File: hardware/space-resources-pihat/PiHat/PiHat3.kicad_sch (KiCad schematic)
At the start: 44 parts, among them J1 GPIO, J10 Conn_01x02_Socket, J11 Conn_01x03_Socket, J12 Conn_01x03_Socket, J13 Conn_01x03_Socket, J14 Conn_01x02_Socket, J2 Conn_01x02_Socket, J3 Conn_01x04_Socket, J4 Conn_01x04_Socket, J5 Conn_01x02_Socket, J6 Conn_01x02_Socket, J7 Conn_01x02_Socket, J8 Conn_01x04_Socket, J9 Conn_01x02_Socket, M1 AO3400A, M3 AO3400A, U1 TPS54560BDDA

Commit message: fix: Changed buck input and output caps for digikey stocked components
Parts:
- removed D3: SMAZ5V1-13-F, Diode_SMD:D_SMA, symbol Device:D_Zener
- C1, C2, C3: value 2.2u -> 10u; footprint Capacitor_SMD:C_0603_1608Metric -> Capacitor_SMD:C_1206_3216Metric_Pad1.33x1.80mm_HandSolder
- C11, C6, C8: footprint Capacitor_SMD:C_1808_4520Metric -> Capacitor_SMD:C_1210_3225Metric_Pad1.33x2.70mm_HandSolder
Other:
- note added: "https://webench.ti.com/appinfo/webench/scripts/SDP.cgi?ID=436553DDC7067EBB"
- note removed: "(https://webench.ti.com/appinfo/webench/scripts/SDP.cgi?ID=436553DDC7067EBB)"

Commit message: fix: Rectified layout to fit properly with Pi4, added various testpoints and optional i2c pullup resistors
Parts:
- removed J3: Conn_01x04_Socket, Connector_JST:JST_EH_B4B-EH-A_1x04_P2.50mm_Vertical, symbol Connector:Conn_01x04_Socket
- added J3: Conn_01x06_Socket, Connector_JST:JST_EH_B6B-EH-A_1x06_P2.50mm_Vertical, symbol Connector:Conn_01x06_Socket
- added TP1: TestPoint, symbol Connector:TestPoint
- renumbered L2 to L1
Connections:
- net 24V: now also TP1.1
- net 3V3: now also J3.3 (Pin_3)
- net 5V: now also J13.2 (Pin_2), J7.2 (Pin_2), J9.2 (Pin_2); no longer J13.1 (Pin_1), J7.1 (Pin_1), J9.1 (Pin_1)
- net GND: now also J10.1 (Pin_1), J13.1 (Pin_1), J14.1 (Pin_1), J3.4 (Pin_4); no longer J10.2 (Pin_2), J13.2 (Pin_2), J14.2 (Pin_2)
- net GPIO17: now also J3.5 (Pin_5)
- net GPIO19/PCM.FS: now also R11.2; no longer R2.2
- net GPIO20/PCM.DIN: no longer R11.2
- net GPIO26: now also R2.2
- net GPIO27: now also J3.6 (Pin_6)
- net GPIO2/SDA1: now also J3.2 (Pin_2)
- net GPIO3/SCL1: now also J3.1 (Pin_1)
- net at R13.1: now also J10.2 (Pin_2); no longer J10.1 (Pin_1)
- net at D2.2 (A), M1.3 (D): now also J7.1 (Pin_1); no longer J7.2 (Pin_2)
- net at M3.3 (D): now also J9.1 (Pin_1); no longer J9.2 (Pin_2)
- net at R15.1: now also J14.2 (Pin_2); no longer J14.1 (Pin_1)
- net BST: now reaches C4.1, U1.1 (BOOT)
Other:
- note added: "Test Points"
- moved on the sheet: J14, J4, L1

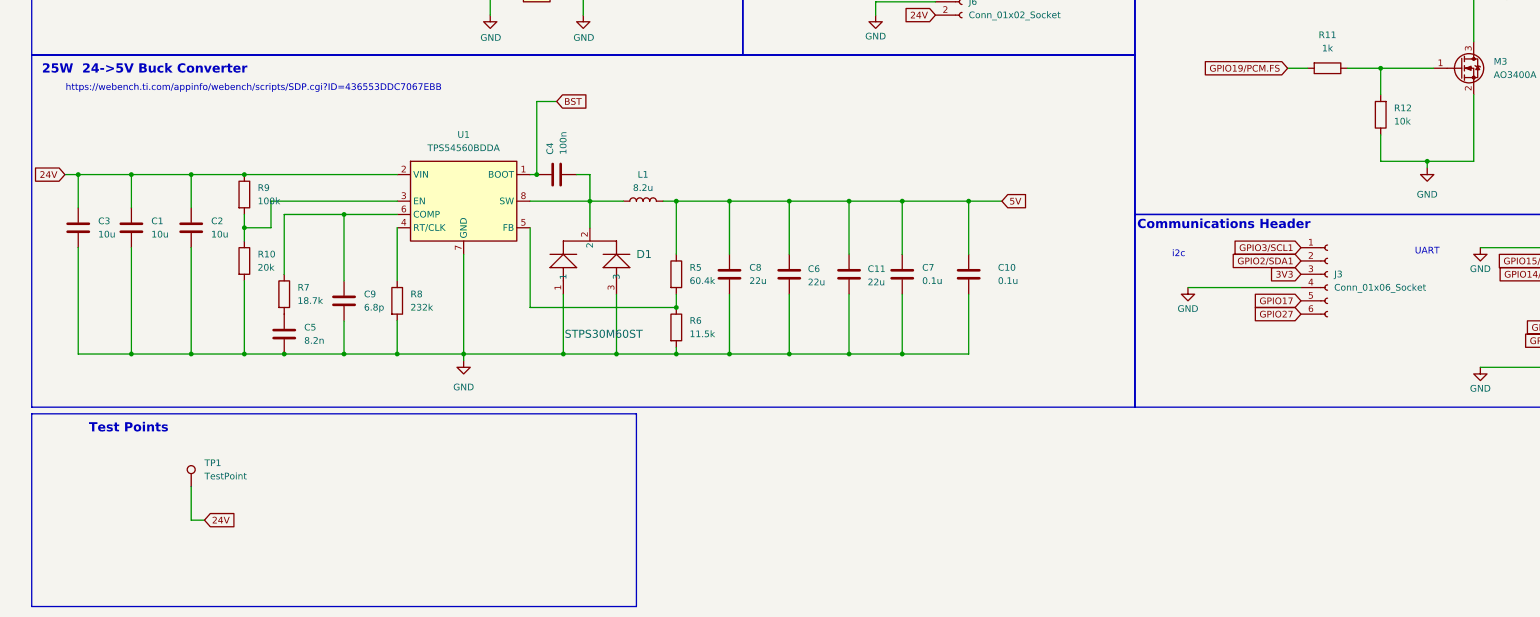
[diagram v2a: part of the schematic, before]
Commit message: small schematic changes
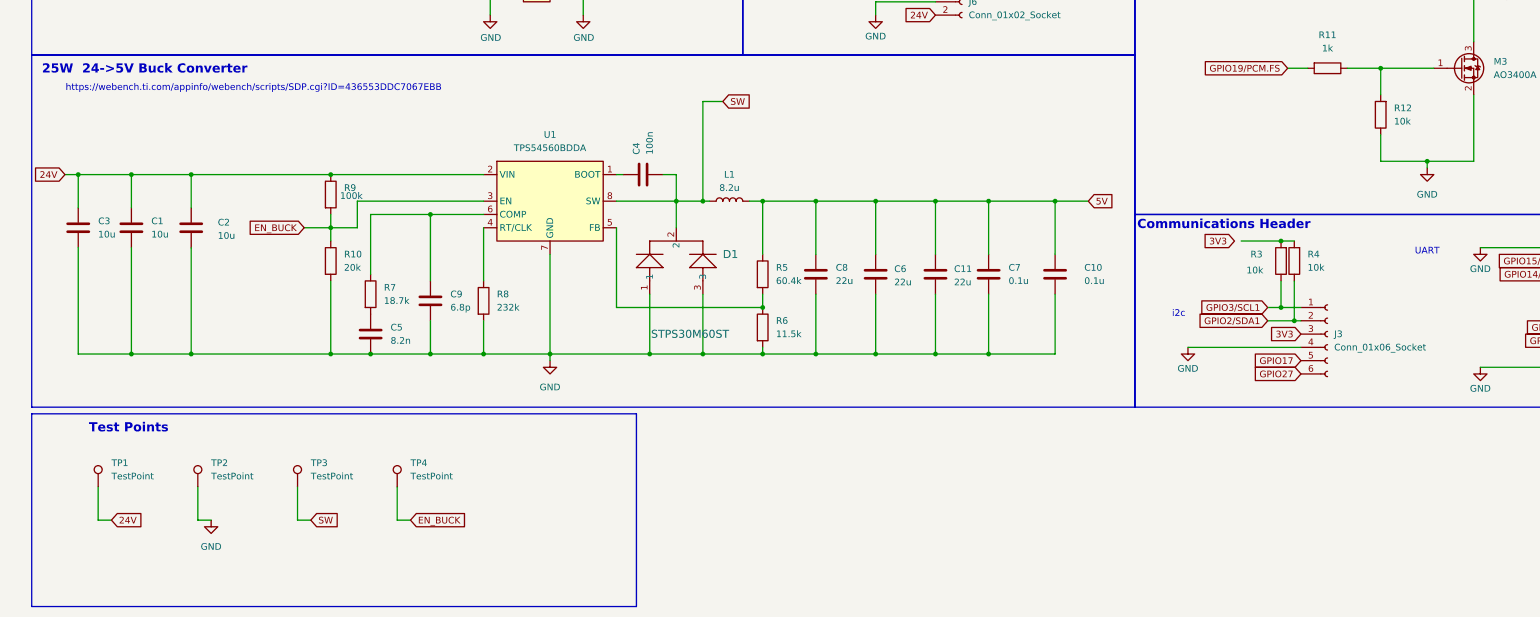
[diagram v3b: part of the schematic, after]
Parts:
- added R3, R4: 10k, Resistor_SMD:R_0603_1608Metric_Pad0.98x0.95mm_HandSolder, symbol Device:R
- added TP2: TestPoint, Connector_Pin:Pin_D1.0mm_L10.0mm, symbol Connector:TestPoint
- added TP3, TP4: TestPoint, Connector_PinHeader_1.00mm:PinHeader_1x01_P1.00mm_Vertical, symbol Connector:TestPoint
- TP1: footprint (none) -> Connector_Pin:Pin_D1.0mm_L10.0mm
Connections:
- net GND: now also TP2.1
- net GPIO2/SDA1: now also R4.1
- net GPIO3/SCL1: now also R3.1
- net SW: now reaches C4.2, D1.2, L1.1, U1.8 (SW)
- net SW: now also TP3.1
- net EN_BUCK: now reaches R10.1, R9.2, U1.3 (EN)
- net EN_BUCK: now also TP4.1
- net BST: no longer names the net of C4.1, U1.1 (BOOT)
- new net: R3.2, R4.2
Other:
- moved on the sheet: C10, C11, C4, C5, C6, C7, C8, C9, D1, J3, L1, R10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

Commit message: fix: Final touchups, ready for order
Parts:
- TP1, TP2: footprint Connector_Pin:Pin_D1.0mm_L10.0mm -> Connector_PinHeader_1.00mm:PinHeader_1x01_P1.00mm_Vertical
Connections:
- net 3V3: now also R3.2, R4.2
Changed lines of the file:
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@@
 	(global_label "3V3"
 		(shape input)
-		(at 243.84 123.19 180)
+		(at 245.11 123.19 180)
 		(fields_autoplaced yes)
 		(effects
@@
 		)
 		(property "Intersheetrefs" "${INTERSHEET_REFS}"
-			(at 237.2521 123.19 0)
+			(at 238.5221 123.19 0)
 			(effects
 				(font
@@
 	)
 	(symbol
+		(lib_id "Connector:TestPoint")
+		(at 26.67 170.18 0)
+		(unit 1)
+		(exclude_from_sim no)
+		(in_bom yes)
+		(on_board yes)
+		(dnp no)
+		(fields_autoplaced yes)
+		(property "Reference" "TP1"
+			(at 29.21 165.6079 0)
+			(effects
+				(font
+					(size 1.27 1.27)
+				)
+				(justify left)
+			)
+		)
+		(property "Value" "TestPoint"
+			(at 29.21 168.1479 0)
+			(effects
+				(font
+					(size 1.27 1.27)
+				)
+				(justify left)
+			)
+		)
+		(property "Footprint" "Connector_PinHeader_1.00mm:PinHeader_1x01_P1.00mm_Vertical"
+			(at 31.75 170.18 0)
+			(effects
+				(font
+					(size 1.27 1.27)
+				)
+				(hide yes)
+			)
+		)
+		(property "Datasheet" "~"
+			(at 31.75 170.18 0)
+			(effects
+				(font
+					(size 1.27 1.27)
+				)
+				(hide yes)
+			)
+		)
+		(property "Description" "test point"
+			(at 26.67 170.18 0)
+			(effects
+				(font
+					(size 1.27 1.27)
+				)
+				(hide yes)
+			)
+		)
+		(pin "1"
+		)
+		(instances
+			(project "PiHat3"
+				(path "/e63e39d7-6ac0-4ffd-8aa3-1841a4541b55"
+					(reference "TP1")
+					(unit 1)
+				)
+			)
+		)
+	)
+	(symbol
 		(lib_id "Device:R")
 		(at 78.74 133.35 0)
@@
 	)
 	(symbol
-		(lib_id "Connector:TestPoint")
-		(at 45.72 170.18 0)
-		(unit 1)
-		(exclude_from_sim no)
-		(in_bom yes)
-		(on_board yes)
-		(dnp no)
-		(fields_autoplaced yes)
-		(property "Reference" "TP2"
-			(at 48.26 165.6079 0)
-			(effects
-				(font
-					(size 1.27 1.27)
-				)
-				(justify left)
-			)
-		)
-		(property "Value" "TestPoint"
-			(at 48.26 168.1479 0)
-			(effects
-				(font
-					(size 1.27 1.27)
-				)
-				(justify left)
-			)
-		)
-		(property "Footprint" "Connector_Pin:Pin_D1.0mm_L10.0mm"
-			(at 50.8 170.18 0)
-			(effects
-				(font
-					(size 1.27 1.27)
-				)
-				(hide yes)
-			)
-		)
-		(property "Datasheet" "~"
-			(at 50.8 170.18 0)
-			(effects
-				(font
-					(size 1.27 1.27)
-				)
-				(hide yes)
-			)
-		)
-		(property "Description" "test point"
-			(at 45.72 170.18 0)
-			(effects
-				(font
-					(size 1.27 1.27)
-				)
-				(hide yes)
-			)
-		)
-		(pin "1"
-		)
-		(instances
-			(project "PiHat3"
-				(path "/e63e39d7-6ac0-4ffd-8aa3-1841a4541b55"
-					(reference "TP2")
-					(unit 1)
-				)
-			)
-		)
-	)
-	(symbol
 		(lib_id "Transistor_FET:AO3400A")
 		(at 287.02 90.17 0)
@@
 	)
 	(symbol
-		(lib_id "Connector:TestPoint")
-		(at 26.67 170.18 0)
+		(lib_id "Device:C")
+		(at 130.81 110.49 90)
 		(unit 1)
 		(exclude_from_sim no)
@@
 		(on_board yes)
 		(dnp no)
-		(fields_autoplaced yes)
-		(property "Reference" "TP1"
-			(at 29.21 165.6079 0)
+		(property "Reference" "C4"
+			(at 129.5399 106.68 0)
 			(effects
 				(font
@@
 			)
 		)
-		(property "Value" "TestPoint"
-			(at 29.21 168.1479 0)
+		(property "Value" "100n"
+			(at 132.0799 106.68 0)
 			(effects
 				(font
@@
 			)
 		)
-		(property "Footprint" "Connector_Pin:Pin_D1.0mm_L10.0mm"
-			(at 31.75 170.18 0)
+		(property "Footprint" "Capacitor_SMD:C_0603_1608Metric"
+			(at 134.62 109.5248 0)
 			(effects
 				(font
@@
 		)
 		(property "Datasheet" "~"
-			(at 31.75 170.18 0)
+			(at 130.81 110.49 0)
 			(effects
 				(font
@@
 			)
 		)
-		(property "Description" "test point"
-			(at 26.67 170.18 0)
+		(property "Description" "Unpolarized capacitor"
+			(at 130.81 110.49 0)
 			(effects
 				(font
@@
 			)
 		)
+		(pin "2"
+		)
 		(pin "1"
 		)
 		(instances
-			(project ""
+			(project "PiHat2"
 				(path "/e63e39d7-6ac0-4ffd-8aa3-1841a4541b55"
-					(reference "TP1")
+					(reference "C4")
 					(unit 1)
 				)
@@
 	)
 	(symbol
-		(lib_id "Device:C")
-		(at 130.81 110.49 90)
+		(lib_id "Connector:TestPoint")
+		(at 45.72 170.18 0)
 		(unit 1)
 		(exclude_from_sim no)
@@
 		(on_board yes)
 		(dnp no)
-		(property "Reference" "C4"
-			(at 129.5399 106.68 0)
+		(fields_autoplaced yes)
+		(property "Reference" "TP2"
+			(at 48.26 165.6079 0)
 			(effects
 				(font
@@
 			)
 		)
-		(property "Value" "100n"
-			(at 132.0799 106.68 0)
+		(property "Value" "TestPoint"
+			(at 48.26 168.1479 0)
 			(effects
 				(font
@@
 			)
 		)
-		(property "Footprint" "Capacitor_SMD:C_0603_1608Metric"
-			(at 134.62 109.5248 0)
+		(property "Footprint" "Connector_PinHeader_1.00mm:PinHeader_1x01_P1.00mm_Vertical"
+			(at 50.8 170.18 0)
 			(effects
 				(font
@@
 		)
 		(property "Datasheet" "~"
-			(at 130.81 110.49 0)
+			(at 50.8 170.18 0)
 			(effects
 				(font
@@
 			)
 		)
-		(property "Description" "Unpolarized capacitor"
-			(at 130.81 110.49 0)
+		(property "Description" "test point"
+			(at 45.72 170.18 0)
 			(effects
 				(font
@@
 			)
 		)
-		(pin "2"
-		)
 		(pin "1"
 		)
 		(instances
-			(project "PiHat2"
+			(project "PiHat3"
 				(path "/e63e39d7-6ac0-4ffd-8aa3-1841a4541b55"
-					(reference "C4")
+					(reference "TP2")
 					(unit 1)
 				)
